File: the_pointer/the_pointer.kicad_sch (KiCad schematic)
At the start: 20 parts, among them U1 ESP32-S3FN8, U10 TPS61033DRLR, U2 W25Q128JVS, X2 XRCGB40M000F1S2GR0

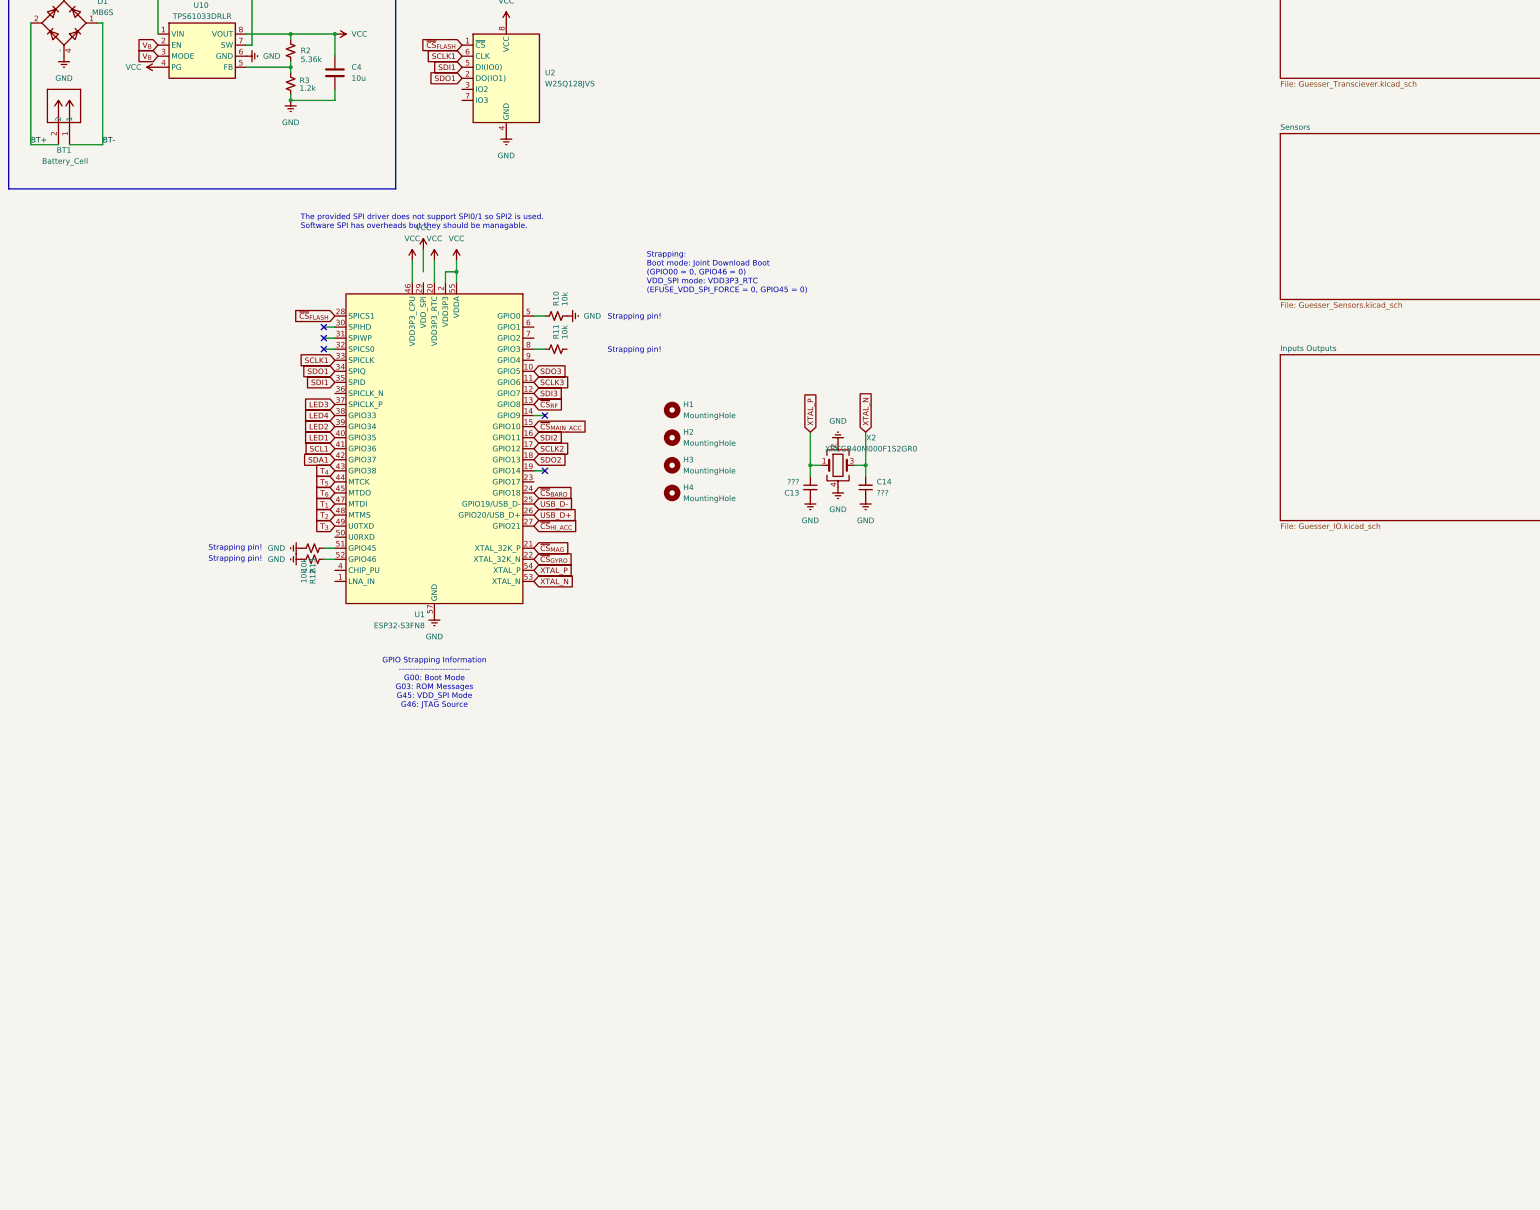
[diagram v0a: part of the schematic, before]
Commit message: Routed Pointer RF transmitter
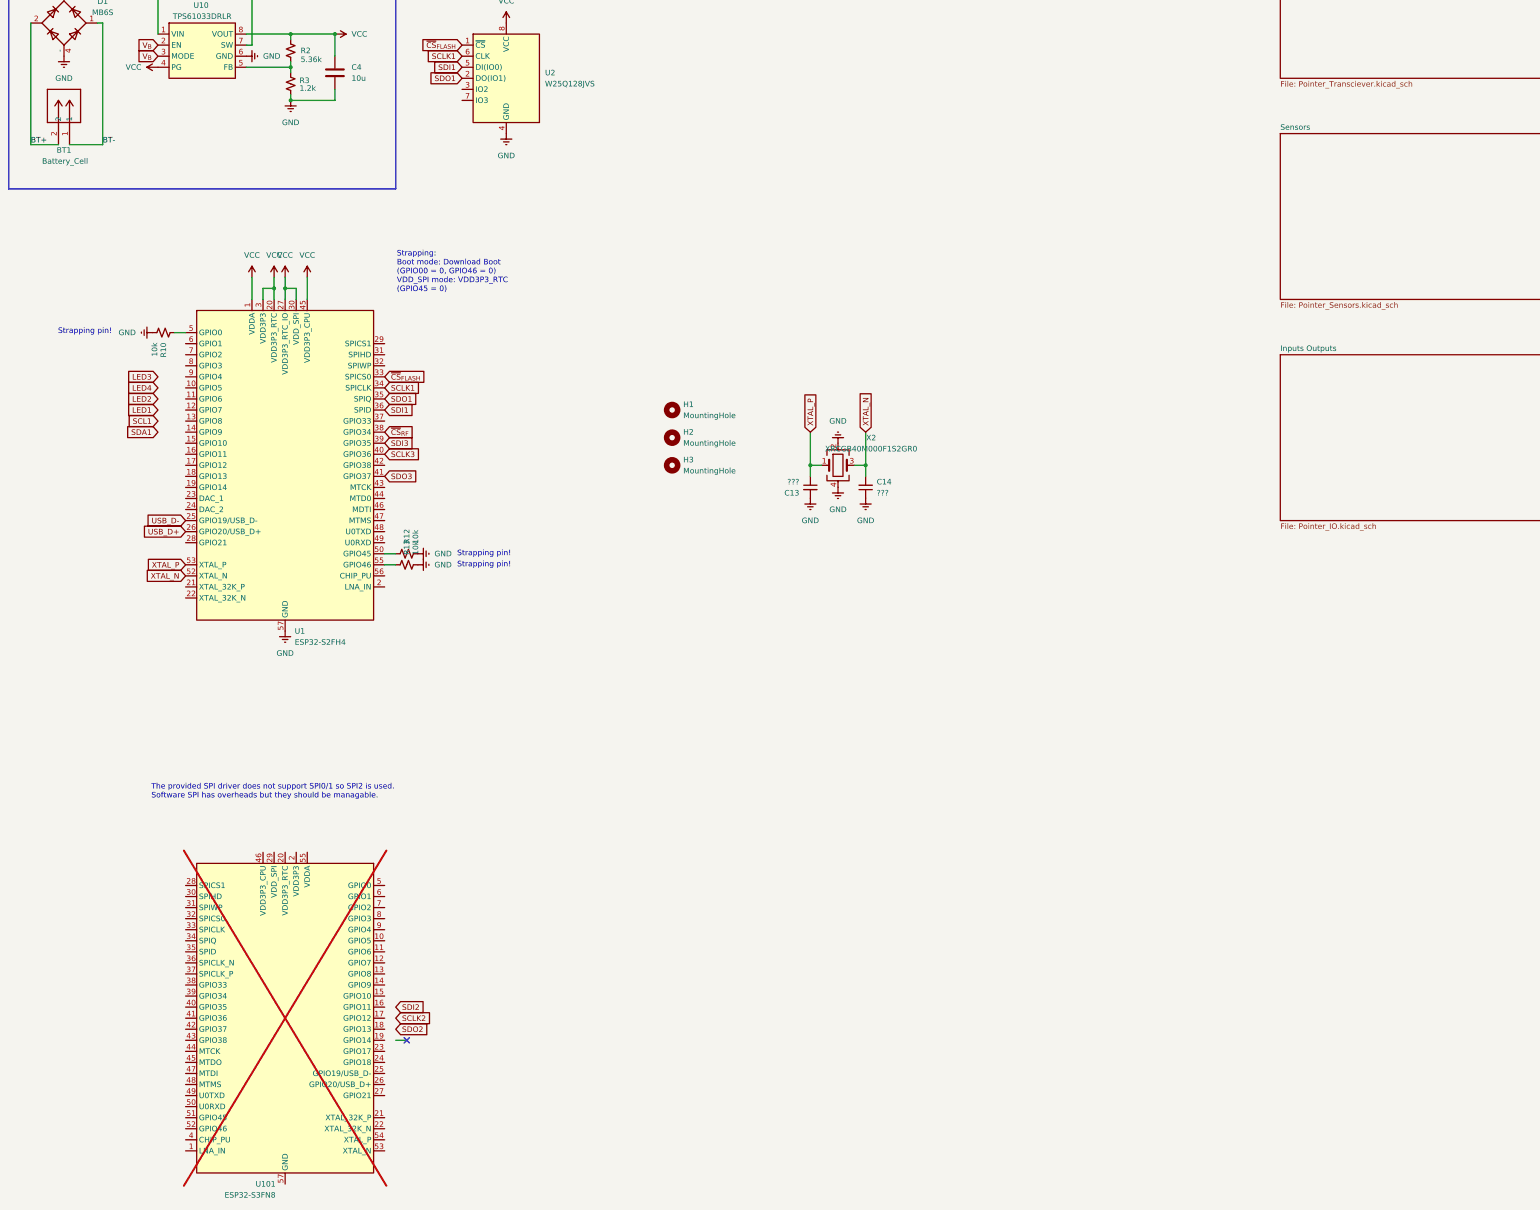
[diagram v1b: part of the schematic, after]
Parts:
- removed H4: MountingHole, MountingHole:MountingHole_3.2mm_M3, symbol Mechanical:MountingHole
- removed R11: 10k, Resistor_SMD:R_0603_1608Metric, symbol Device:R_Small_US
- added U1: ESP32-S2FH4, Package_DFN_QFN:QFN-56-1EP_7x7mm_P0.4mm_EP4x4mm, symbol MCU_Espressif:ESP32-S2
- U101: renamed from U1; now not fitted; now left out of the parts list
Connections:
- net GND: now also U1.57 (GND); no longer U101.57 (GND)
- net LED1: no longer U101.40 (GPIO35)
- net LED2: no longer U101.39 (GPIO34)
- net LED3: no longer U101.37 (SPICLK_P)
- net LED4: no longer U101.38 (GPIO33)
- net SCL1: no longer U101.41 (GPIO36)
- net SCLK1: now also U1.34 (SPICLK); no longer U101.33 (SPICLK)
- net SCLK2: no longer U101.17 (GPIO12)
- net SCLK3: now also U1.40 (GPIO36); no longer U101.11 (GPIO6)
- net SDA1: no longer U101.42 (GPIO37)
- net SDI1: now also U1.36 (SPID); no longer U101.35 (SPID)
- net SDI2: no longer U101.16 (GPIO11)
- net SDI3: now also U1.39 (GPIO35); no longer U101.12 (GPIO7)
- net SDO1: now also U1.35 (SPIQ); no longer U101.34 (SPIQ)
- net SDO2: no longer U101.18 (GPIO13)
- net SDO3: now also U1.41 (GPIO37); no longer U101.10 (GPIO5)
- net USB_D+: now also U1.26 (GPIO20/USB_D+); no longer U101.26 (GPIO20/USB_D+)
- net USB_D-: now also U1.25 (GPIO19/USB_D-); no longer U101.25 (GPIO19/USB_D-)
- net VCC: now also U1.1 (VDDA), U1.20 (VDD3P3_RTC), U1.27 (VDD3P3_RTC_IO), U1.3 (VDD3P3), U1.30 (VDD_SPI), U1.4 (VDD3P3), U1.45 (VDD3P3_CPU), U1.51 (VDDA), U1.54 (VDDA); no longer U101.2 (VDD3P3), U101.20 (VDD3P3_RTC), U101.3 (VDD3P3), U101.46 (VDD3P3_CPU), U101.55 (VDDA), U101.56 (VDDA)
- net XTAL_N: now also U1.52 (XTAL_N); no longer U101.53 (XTAL_N)
- net XTAL_P: now also U1.53 (XTAL_P); no longer U101.54 (XTAL_P)
- net ~{CS}_{FLASH}: now also U1.33 (SPICS0); no longer U101.28 (SPICS1)
- net ~{CS}_{RF}: now also U1.38 (GPIO34); no longer U101.13 (GPIO8)
- net at R10.1: now also U1.5 (GPIO0); no longer U101.5 (GPIO0)
- net at R12.1: now also U1.50 (GPIO45); no longer U101.52 (GPIO46)
- net at U101.51 (GPIO45): no longer R13.1
- net T_{1}: no longer names the net of U101.47 (MTDI)
- net T_{2}: no longer names the net of U101.48 (MTMS)
- net T_{3}: no longer names the net of U101.49 (U0TXD)
- net T_{4}: no longer names the net of U101.43 (GPIO38)
- net T_{5}: no longer names the net of U101.44 (MTCK)
- net T_{6}: no longer names the net of U101.45 (MTDO)
- net ~{CS}_{BARO}: no longer names the net of U101.24 (GPIO18)
- net ~{CS}_{GYRO}: no longer names the net of U101.22 (XTAL_32K_N)
- net ~{CS}_{HI_ACC}: no longer names the net of U101.27 (GPIO21)
- net ~{CS}_{MAG}: no longer names the net of U101.21 (XTAL_32K_P)
- net ~{CS}_{MAIN_ACC}: no longer names the net of U101.15 (GPIO10)
- new net: U101.2 (VDD3P3), U101.3 (VDD3P3)
- new net: U101.55 (VDDA), U101.56 (VDDA)
- new net: R13.1, U1.55 (GPIO46)
- no-connect marks 5 -> 1
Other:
- sheet Inputs Outputs: file Guesser_IO.kicad_sch -> Pointer_IO.kicad_sch
- sheet Sensors: file Guesser_Sensors.kicad_sch -> Pointer_Sensors.kicad_sch
- sheet Transmitter: file Guesser_Transciever.kicad_sch -> Pointer_Transciever.kicad_sch
- note added: "Strapping: Boot mode: Download Boot (GPIO00 = 0, GPIO46 = 0) VDD_SPI mode: VDD3P3_RTC (GPIO45 = 0)"
- note removed: "GPIO Strapping Information -------------------------- G00: Boot Mode G03: ROM Messages G45: VDD_SPI Mode G46: JTAG Source"
- note removed: "Strapping: Boot mode: Joint Download Boot (GPIO00 = 0, GPIO46 = 0) VDD_SPI mode: VDD3P3_RTC (EFUSE_VDD_SPI_FORCE = 0, GPIO45 = 0)"
- moved on the sheet: R10, R12, R13

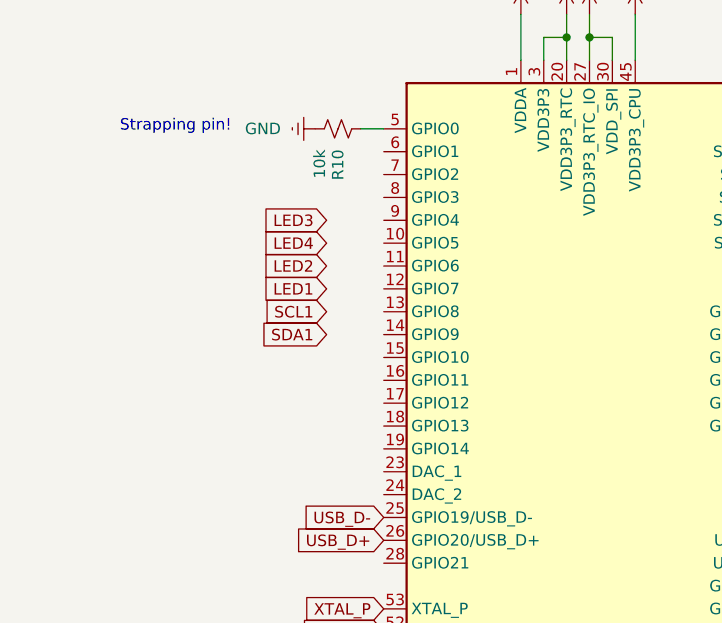
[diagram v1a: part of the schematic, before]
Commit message: Routed Pointer GPS
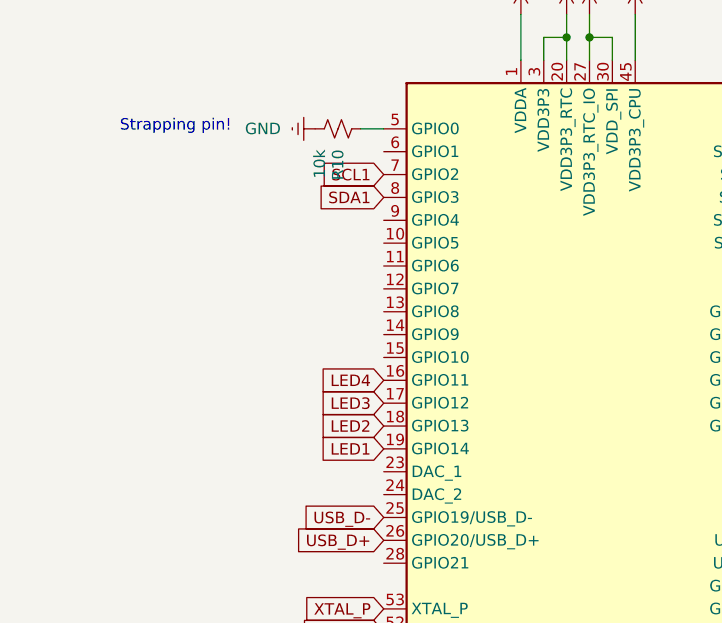
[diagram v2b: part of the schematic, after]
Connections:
- net LED1: now also U1.19 (GPIO14)
- net LED2: now also U1.18 (GPIO13)
- net LED3: now also U1.17 (GPIO12)
- net LED4: now also U1.16 (GPIO11)
- net SCL1: now also U1.7 (GPIO2)
- net SDA1: now also U1.8 (GPIO3)
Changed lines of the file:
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@@
 	(global_label "LED2"
 		(shape input)
-		(at 46.99 124.46 180)
-		(fields_autoplaced yes)
-		(effects
-			(font
-				(size 1.27 1.27)
-			)
-			(justify right)
-		)
-		(property "Intersheetrefs" "${INTERSHEET_REFS}"
-			(at 39.3482 124.46 0)
+		(at 53.34 142.24 180)
+		(fields_autoplaced yes)
+		(effects
+			(font
+				(size 1.27 1.27)
+			)
+			(justify right)
+		)
+		(property "Intersheetrefs" "${INTERSHEET_REFS}"
+			(at 45.6982 142.24 0)
 			(effects
 				(font
@@
 	(global_label "LED3"
 		(shape input)
-		(at 46.99 119.38 180)
-		(fields_autoplaced yes)
-		(effects
-			(font
-				(size 1.27 1.27)
-			)
-			(justify right)
-		)
-		(property "Intersheetrefs" "${INTERSHEET_REFS}"
-			(at 39.3482 119.38 0)
+		(at 53.34 139.7 180)
+		(fields_autoplaced yes)
+		(effects
+			(font
+				(size 1.27 1.27)
+			)
+			(justify right)
+		)
+		(property "Intersheetrefs" "${INTERSHEET_REFS}"
+			(at 45.6982 139.7 0)
 			(effects
 				(font
@@
 	(global_label "LED4"
 		(shape input)
-		(at 46.99 121.92 180)
-		(fields_autoplaced yes)
-		(effects
-			(font
-				(size 1.27 1.27)
-			)
-			(justify right)
-		)
-		(property "Intersheetrefs" "${INTERSHEET_REFS}"
-			(at 39.3482 121.92 0)
+		(at 53.34 137.16 180)
+		(fields_autoplaced yes)
+		(effects
+			(font
+				(size 1.27 1.27)
+			)
+			(justify right)
+		)
+		(property "Intersheetrefs" "${INTERSHEET_REFS}"
+			(at 45.6982 137.16 0)
 			(effects
 				(font
@@
 	(global_label "SDA1"
 		(shape input)
-		(at 46.99 132.08 180)
-		(fields_autoplaced yes)
-		(effects
-			(font
-				(size 1.27 1.27)
-			)
-			(justify right)
-		)
-		(property "Intersheetrefs" "${INTERSHEET_REFS}"
-			(at 39.2272 132.08 0)
+		(at 53.34 116.84 180)
+		(fields_autoplaced yes)
+		(effects
+			(font
+				(size 1.27 1.27)
+			)
+			(justify right)
+		)
+		(property "Intersheetrefs" "${INTERSHEET_REFS}"
+			(at 45.5772 116.84 0)
 			(effects
 				(font
@@
 	(global_label "LED1"
 		(shape input)
-		(at 46.99 127 180)
-		(fields_autoplaced yes)
-		(effects
-			(font
-				(size 1.27 1.27)
-			)
-			(justify right)
-		)
-		(property "Intersheetrefs" "${INTERSHEET_REFS}"
-			(at 39.3482 127 0)
+		(at 53.34 144.78 180)
+		(fields_autoplaced yes)
+		(effects
+			(font
+				(size 1.27 1.27)
+			)
+			(justify right)
+		)
+		(property "Intersheetrefs" "${INTERSHEET_REFS}"
+			(at 45.6982 144.78 0)
 			(effects
 				(font
@@
 	(global_label "SCL1"
 		(shape input)
-		(at 46.99 129.54 180)
-		(fields_autoplaced yes)
-		(effects
-			(font
-				(size 1.27 1.27)
-			)
-			(justify right)
-		)
-		(property "Intersheetrefs" "${INTERSHEET_REFS}"
-			(at 39.2877 129.54 0)
-			(effects
-				(font
+		(at 53.34 114.3 180)
+		(fields_autoplaced yes)
+		(effects
+			(font
+				(size 1.27 1.27)
+			)
+			(justify right)
+		)
+		(property "Intersheetrefs" "${INTERSHEET_REFS}"
+			(at 45.6377 114.3 0)
+			(effects
+				(font
